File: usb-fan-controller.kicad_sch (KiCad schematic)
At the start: 120 parts, among them J1 1054500101, J10 JTAG_CONN, J11 DATA_CONN, J12 BOOT0_MODE, J2 EXTPWR_JACK, J3 EXTPWR, J4 PWR_LED, J5 VBAT, J6 THERMO1, J7 THERMO2, J8 SYS_LED, J9 BOOT1_MODE, M1 470531000, M2 470531000, Q1 2N7002, Q2 2N7002, Q3 AO3401A, Q4 2N7002, Q5 2N7002, Q6 AO3401A, Q7 2N7002, Q8 2N7002, SW1 SW_RESET, U1 TPS61040DBV, U2 BQ24392RSER, U3 SRV05-4-P-T7, U4 HT7533-1, U5 MAX6675ISA+, U6 STM32F103C8T6, U7 MAX6675ISA+, Y1 32.768Hz@12.5pF, Y2 8MHz@20pF

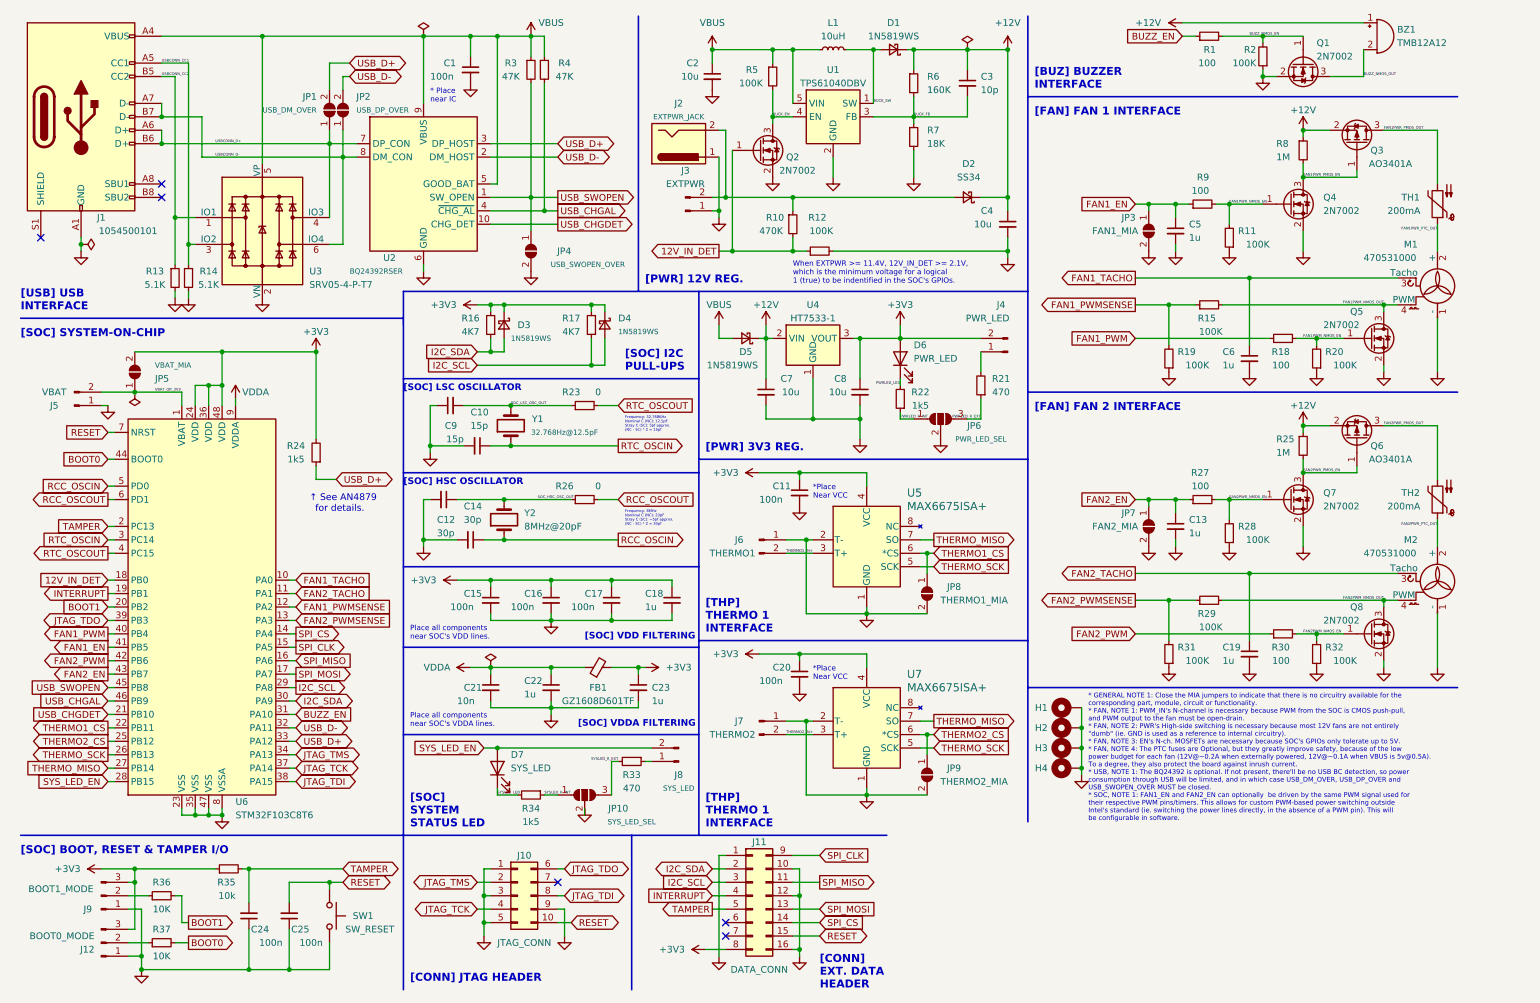
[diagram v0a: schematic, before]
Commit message: feat: add external THM SPI connection
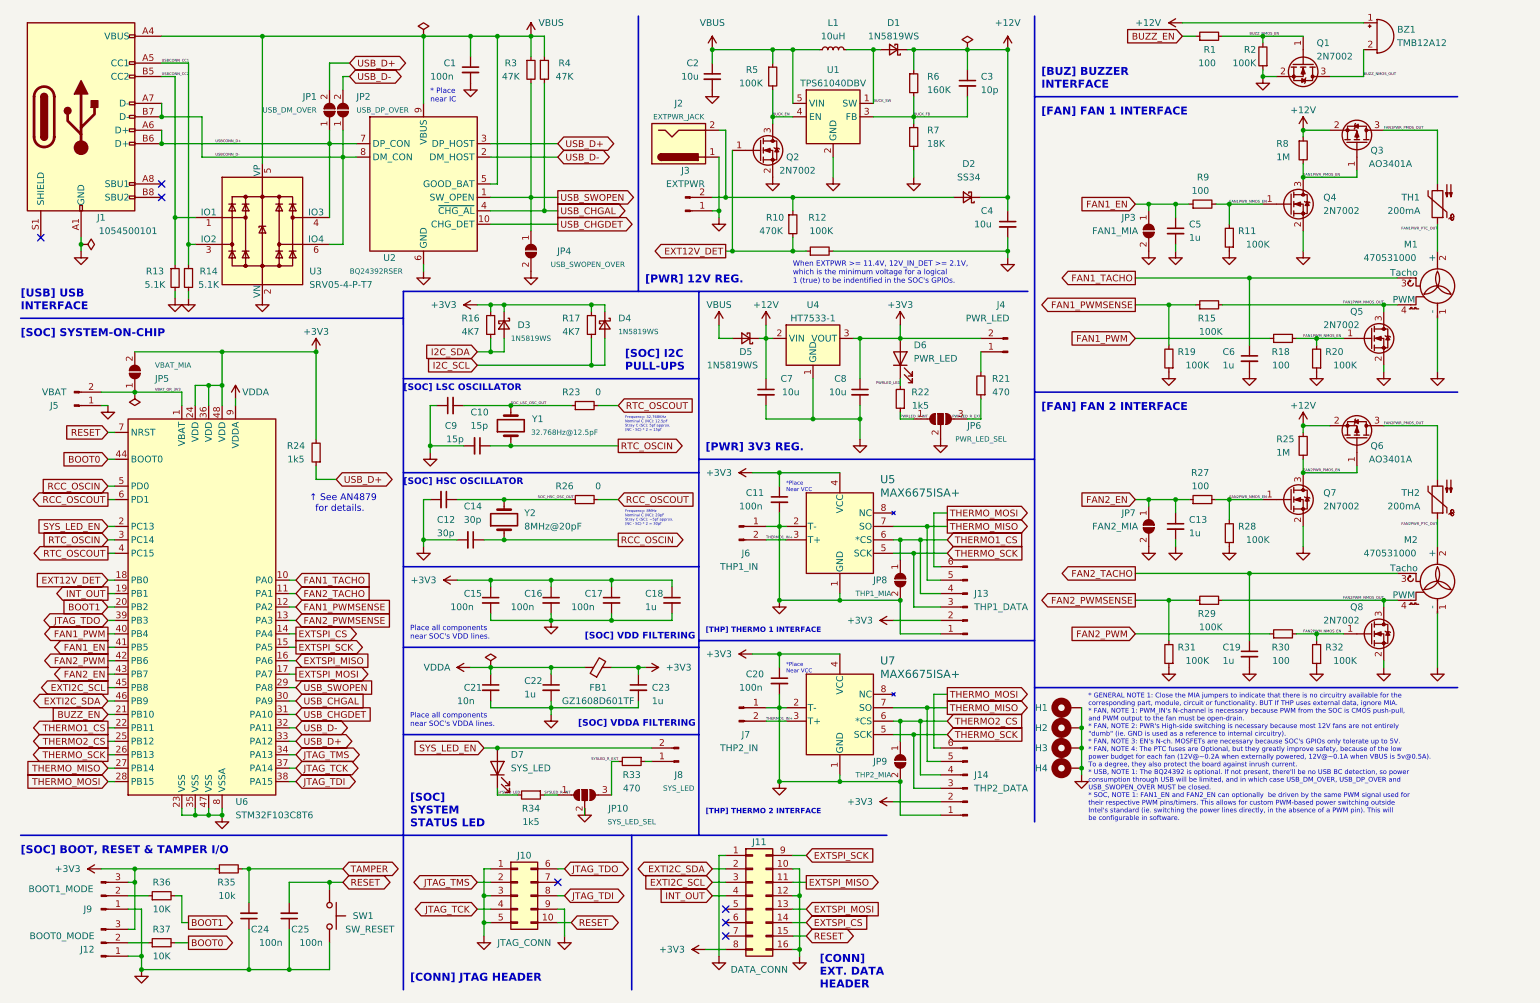
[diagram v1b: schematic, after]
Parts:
- added J13: THP1_DATA, symbol Connector:Conn_01x06_Male
- added J14: THP2_DATA, Connector_PinHeader_2.54mm:PinHeader_1x06_P2.54mm_Horizontal, symbol Connector:Conn_01x06_Male
- J10: footprint (none) -> Connector_PinHeader_2.54mm:PinHeader_2x05_P2.54mm_Horizontal
- J6: value THERMO1 -> THP1_IN
- J7: value THERMO2 -> THP2_IN
- JP8: value THERMO1_MIA -> THP1_MIA
- JP9: value THERMO2_MIA -> THP2_MIA
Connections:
- net THERMO2_IN+ is gone; now on net THERMO1_IN+: J7.2 (Pin_2), U7.3 (T+)
- net +3V3: now also J13.2 (Pin_2), J14.2 (Pin_2)
- net BUZZ_EN: now also U6.21 (PB10); no longer U6.31 (PA10)
- net GND: now also J13.1 (Pin_1), J14.1 (Pin_1)
- net I2C_SCL: no longer J11.3 (Pin_3), U6.29 (PA8)
- net I2C_SDA: no longer J11.2 (Pin_2), U6.30 (PA9)
- net SYS_LED_EN: now also U6.2 (PC13); no longer U6.28 (PB15)
- net TAMPER: no longer J11.5 (Pin_5), U6.2 (PC13)
- net THERMO1_CS: now also J13.4 (Pin_4)
- net THERMO2_CS: now also J14.4 (Pin_4)
- net THERMO_MISO: now also J13.5 (Pin_5), J14.5 (Pin_5)
- net THERMO_SCK: now also J13.3 (Pin_3), J14.3 (Pin_3)
- net USB_CHGAL: now also U6.30 (PA9); no longer U6.46 (PB9)
- net USB_CHGDET: now also U6.31 (PA10); no longer U6.21 (PB10)
- net USB_SWOPEN: now also U6.29 (PA8); no longer U6.45 (PB8)
- net 12V_IN_DET renamed EXT12V_DET
- net INTERRUPT renamed INT_OUT
- net SPI_CLK renamed EXTSPI_SCK
- net SPI_CS renamed EXTSPI_CS
- net SPI_MISO renamed EXTSPI_MISO
- net SPI_MOSI renamed EXTSPI_MOSI
- new net EXTI2C_SCL: J11.3 (Pin_3), U6.45 (PB8)
- new net EXTI2C_SDA: J11.2 (Pin_2), U6.46 (PB9)
- new net THERMO_MOSI: J13.6 (Pin_6), J14.6 (Pin_6), U6.28 (PB15)
- no-connect marks 6 -> 7
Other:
- note added: "* GENERAL NOTE 1: Close the MIA jumpers to indicate that there is no circuitry available for the corresponding part, module, circuit or functionality. BUT If THP uses external data, ignore MIA. * FAN, NOTE 1: PWM_IN's N-channel is necessary because PWM from the SOC is CMOS push-pull, and PWM output to the fan must be open-drain. * FAN, NOTE 2: PWR's High-side switching is necessary because most 1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"
- note added: "[THP] THERMO 2 INTERFACE"
- note removed: "* GENERAL NOTE 1: Close the MIA jumpers to indicate that there is no circuitry available for the corresponding part, module, circuit or functionality. * FAN, NOTE 1: PWM_IN's N-channel is necessary because PWM from the SOC is CMOS push-pull, and PWM output to the fan must be open-drain. * FAN, NOTE 2: PWR's High-side switching is necessary because most 12V fans are not entirely "dumb" (ie. GND is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"
- moved on the sheet: C11, J6, JP8, U5
